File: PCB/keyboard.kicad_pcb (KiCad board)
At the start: 2 copper layers, 173 parts, among them J1 SW_Push, K1 SW_Push, M1 SW_Push, P1 SW_Push, Q1 SW_Push, SW1 RotaryEncoder_Switch, T1 SW_Push, U1 Pico, U2 SW_Push, X1 SW_Push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

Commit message: Got rid of extra unnecessary key
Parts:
- removed D75: D_Small, Diode_SMD:D_SOD-123
- removed SCREEN1: SW_Push, Button_Switch_Keyboard:SW_Cherry_MX_1.00u_PCB

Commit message: Moved diodes into position
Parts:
- moved D84 213.4 mm to (361.3, 54.0)
- moved D81 199.6 mm to (361.7, 73.0)
- moved D85 199.0 mm to (341.6, 54.0)
- moved D72 188.5 mm to (360.7, 130.2)
- moved D86 186.2 mm to (322.6, 54.0)
- moved D82 183.6 mm to (341.6, 72.4)
- moved D63 179.8 mm to (275.6, 29.8)
- moved D69 173.3 mm to (295.3, 29.8)
- moved D83 170.1 mm to (323.9, 72.4)
- moved D80 167.5 mm to (342.9, 111.1)
- moved D76 166.4 mm to (285.1, 53.3)
- moved D1 164.6 mm to (29.3, 30.5)
- moved D79 163.1 mm to (342.9, 130.2)
- moved D51 160.5 mm to (238.8, 29.8)
- moved D7 159.8 mm to (67.3, 29.8)
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
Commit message: Wired rows and columns together
I pretty much did the process of hooking each key and diode up to each row and collumn. I haven't attached them to the Raspberrry Pi Pico 2W yet, but that will come next.
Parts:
- U1: moved to B.Cu
- moved U1 60.8 mm to (336.3, 84.5), turned to 90 degrees
- moved D82 11.7 mm to (344.2, 61.0), turned to -90 degrees
- moved D81 11.5 mm to (363.2, 61.6), turned to -90 degrees
- moved D83 11.0 mm to (325.8, 61.6), turned to -90 degrees
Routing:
- net ROW1: track 0.00 -> 378.0 mm, vias 0 -> 15
- net ROW4: track 0.00 -> 369.5 mm, vias 0 -> 14
- net ROW0: track 0.00 -> 362.6 mm, vias 0 -> 14
- net ROW2: track 0.00 -> 310.7 mm, vias 0 -> 14
- net ROW3: track 0.00 -> 286.2 mm, vias 0 -> 13
- net ROW5: track 0.00 -> 267.2 mm
- net COL12: track 0.00 -> 181.9 mm
- net COL11: track 0.00 -> 145.5 mm
- net COL13: track 0.00 -> 134.7 mm
- net COL9: track 0.00 -> 134.0 mm
- net COL10: track 0.00 -> 133.9 mm
- net COL5: track 0.00 -> 126.1 mm
- net COL1: track 0.00 -> 121.7 mm
- net COL2: track 0.00 -> 121.2 mm
- net COL8: track 0.00 -> 108.5 mm
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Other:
- board text added: "Pico HERE"

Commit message: All rows connected
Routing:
- net ROW1: track 378.0 -> 455.0 mm, vias 15 -> 17
- net ROW4: track 369.5 -> 434.5 mm, vias 14 -> 16
- net ROW5: track 267.2 -> 324.3 mm, vias 0 -> 2
- net ROW2: track 310.7 -> 365.1 mm, vias 14 -> 16
- net COL12: track 181.9 -> 235.8 mm, vias 0 -> 2
- net ROW3: track 286.2 -> 339.6 mm, vias 13 -> 14
- net ROW0: track 362.6 -> 410.7 mm, vias 14 -> 18

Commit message: Completed PCB
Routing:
- net COL0: track 107.9 -> 483.5 mm, vias 0 -> 1
- net COL1: track 121.7 -> 457.3 mm, vias 0 -> 1
- net COL3: track 96.7 -> 388.0 mm, vias 0 -> 2
- net COL2: track 121.2 -> 384.1 mm, vias 0 -> 3
- net COL5: track 126.1 -> 335.8 mm, vias 0 -> 3
- net COL4: track 96.7 -> 303.0 mm, vias 0 -> 1
- net COL6: track 105.5 -> 290.7 mm, vias 0 -> 1
- net COL7: track 106.1 -> 270.4 mm, vias 0 -> 2
- net COL10: track 133.9 -> 293.9 mm, vias 0 -> 2
- net COL9: track 134.0 -> 281.8 mm, vias 0 -> 4
- net COL8: track 108.5 -> 256.0 mm, vias 0 -> 2
- net /OLED_SCL: track 0.00 -> 120.8 mm, vias 0 -> 5
- net Net-(OLED DISPLAY1-Pin_2): track 0.00 -> 113.3 mm, vias 0 -> 1
- net ROW5: track 324.3 -> 430.3 mm, vias 2 -> 4
- net /OLED_SDA: track 0.00 -> 105.5 mm, vias 0 -> 4
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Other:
- board outline added: 358.1 x 123.2 mm

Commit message: Fixed a bunch of key spacing issues
I put in some more work on the case, then realized that if the keys are too close on the pcb, the keycaps wont fit (i was worried about larger keys like shift, and how far they should be spaced from the letter keys). i did some googling, and realized that there is an actual grid system for this, and I had completely ignored this when placing keys on my PCB. I had to go back over every key and measure the correct distances, then adjust the switch position accordingly. It was a lot of tedious work, but it payed off. It would have sucked to order the PCB and have none of the keycaps fit.
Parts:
- moved D74 5.97 mm to (290.4, 130.2)
- moved D62 5.72 mm to (241.9, 130.2)
- moved D56 5.33 mm to (219.1, 130.2)
- moved D68 5.33 mm to (265.7, 130.2)
- moved MACRO1 4.76 mm to (262.1, 116.4)
- moved rALT1 4.76 mm to (214.5, 116.4)
- moved rCTRL1 4.76 mm to (285.9, 116.4)
- moved rSHIFT1 4.76 mm to (269.2, 97.3)
- moved rWIN1 4.76 mm to (238.3, 116.4)
- moved BSLASH1 2.38 mm to (285.9, 59.2)
- moved SHIFT1 2.38 mm to (31.1, 97.3)
- moved SPACE1 2.38 mm to (143.0, 116.4)
- moved D5 1.62 mm to (37.4, 111.1)
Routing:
- net COL9: track 281.8 -> 275.1 mm
- net COL12: track 235.8 -> 231.1 mm
- net COL11: track 235.1 -> 231.6 mm, vias 4 -> 3
- net ROW5: track 430.3 -> 433.1 mm
- net COL5: track 335.8 -> 333.7 mm
- net COL10: track 293.9 -> 295.8 mm
- net COL0: track 483.5 -> 481.6 mm
- net ROW4: track 474.3 -> 475.9 mm
- net Net-(D24-K): track 15.6 -> 14.6 mm
- net Net-(D77-K): track 14.7 -> 13.9 mm
- net Net-(D74-K): track 14.5 -> 15.0 mm
- net Net-(D56-K): track 14.8 -> 15.0 mm, vias 0 -> 1

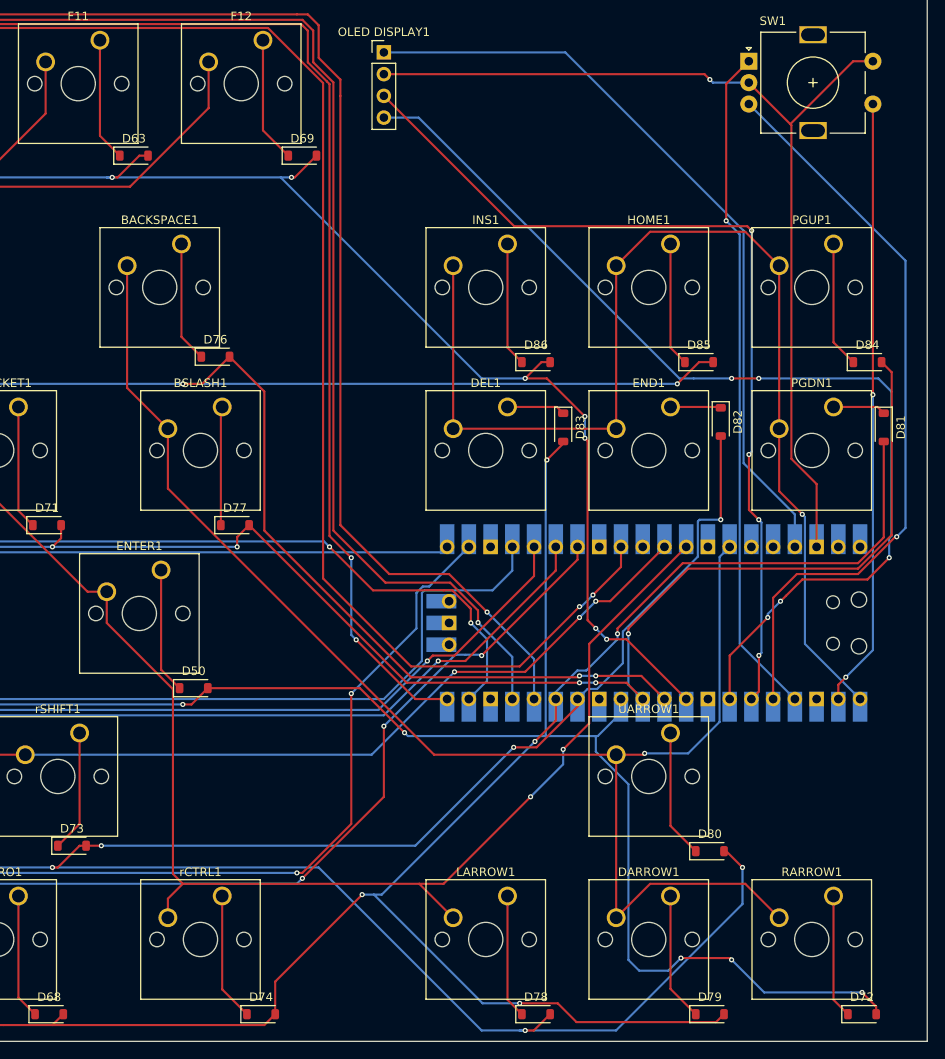
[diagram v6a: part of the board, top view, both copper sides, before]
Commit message: Added top cover and PCB Adjustments
moved home and arrow keys left to fit the standard ANSI grid
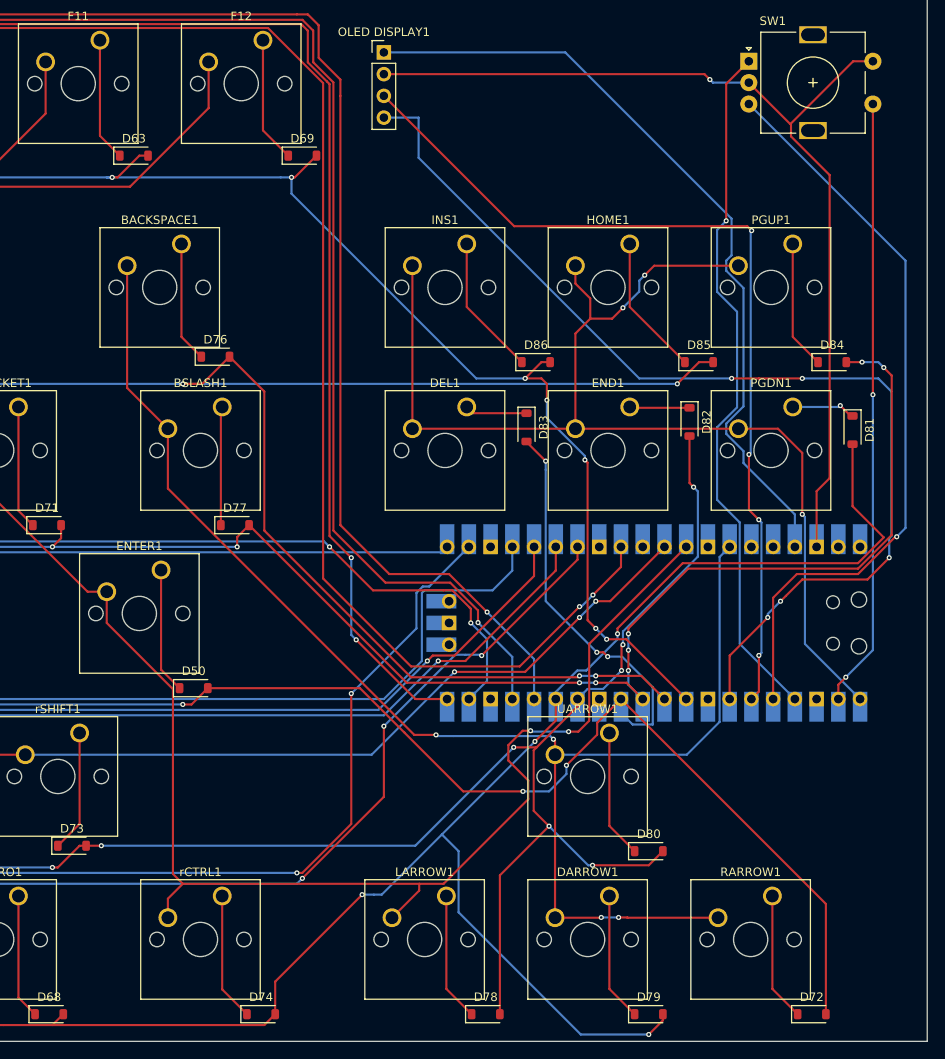
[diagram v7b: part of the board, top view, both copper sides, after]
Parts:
- moved DARROW1 7.14 mm to (331.2, 116.4)
- moved RARROW1 7.14 mm to (350.2, 116.4)
- moved UARROW1 7.14 mm to (331.2, 97.3)
- moved D79 7.14 mm to (335.8, 130.2)
- moved D80 7.14 mm to (335.8, 111.1)
- moved LARROW1 7.14 mm to (312.1, 116.4)
- moved D72 5.87 mm to (354.8, 130.2)
- moved D78 5.87 mm to (316.7, 130.2)
- moved DEL1 4.76 mm to (314.5, 59.2)
- moved END1 4.76 mm to (333.5, 59.2)
- moved HOME1 4.76 mm to (333.5, 40.2)
- moved INS1 4.76 mm to (314.5, 40.2)
- moved PGDN1 4.76 mm to (352.6, 59.2)
- moved PGUP1 4.76 mm to (352.6, 40.2)
- moved D83 4.29 mm to (321.5, 61.6)
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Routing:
- net ROW4: track 475.9 -> 418.3 mm, vias 17 -> 19
- net COL12: track 231.1 -> 236.7 mm
- net ROW5: track 433.1 -> 427.9 mm
- net COL14: track 134.0 -> 138.5 mm, vias 1 -> 3
- net ROW2: track 430.0 -> 433.9 mm, vias 17 -> 21
- net Net-(U1-GPIO2): track 79.0 -> 81.8 mm
- net /OLED_SCL: track 120.8 -> 123.5 mm
- net ROW3: track 436.0 -> 438.7 mm
- net COL13: track 169.3 -> 167.0 mm, vias 1 -> 4
- net Net-(OLED DISPLAY1-Pin_1): track 90.1 -> 92.3 mm
- net Net-(D86-K): track 14.5 -> 16.5 mm
- net Net-(D85-K): track 14.5 -> 16.5 mm
- net Net-(D81-K): track 6.18 -> 7.55 mm, vias 0 -> 1
- net Net-(OLED DISPLAY1-Pin_2): track 113.3 -> 114.4 mm
- net Net-(D82-K): track 5.91 -> 7.02 mm
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
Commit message: Redid PCB bottom two rows
Fixed spacing issues and rewired nodes
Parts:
- moved COMMA1 4.76 mm to (200.2, 97.3)
- moved N10 4.76 mm to (162.1, 97.3)
- moved C1 4.76 mm to (104.9, 97.3)
- moved V1 4.76 mm to (124.0, 97.3)
- moved X1 4.76 mm to (85.9, 97.3)
- moved SHIFT1 4.76 mm to (35.9, 97.3)
- moved Z1 4.76 mm to (66.8, 97.3)
- moved B1 4.76 mm to (143.0, 97.3)
- moved M1 4.76 mm to (181.1, 97.3)
- moved PERIOD1 4.76 mm to (219.2, 97.3)
- moved SLASH1 4.76 mm to (238.3, 97.3)
- moved rSHIFT1 4.76 mm to (274.0, 97.3)
- moved DARROW1 2.38 mm to (333.5, 116.4)
- moved MACRO1 2.38 mm to (264.5, 116.4)
- moved RARROW1 2.38 mm to (352.6, 116.4)
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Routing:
- net ROW3: track 438.7 -> 446.2 mm
- net COL10: track 295.8 -> 303.0 mm
- net COL7: track 270.4 -> 265.8 mm
- net COL6: track 290.7 -> 286.1 mm
- net COL9: track 275.1 -> 278.5 mm, vias 4 -> 3
- net COL1: track 457.3 -> 460.6 mm
- net COL8: track 256.0 -> 252.7 mm
- net COL2: track 384.1 -> 387.1 mm
- net COL0: track 481.6 -> 484.5 mm
- net COL5: track 333.7 -> 331.3 mm
- net Net-(D73-K): track 14.2 -> 16.2 mm
- net COL4: track 303.0 -> 305.0 mm
- net COL3: track 388.0 -> 390.0 mm
- net Net-(D5-K): track 15.7 -> 13.9 mm
- net Net-(D11-K): track 15.6 -> 14.0 mm
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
